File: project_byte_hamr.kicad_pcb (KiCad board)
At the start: 4 copper layers, 125.8 x 84.7 mm, 93 parts, among them J3 Bus_Apple_II_Card_Side, J4 CONN_02X03, U1 LFE5U-25F-6BG381C, U10 IS25LP128F-JBLE, U11 SN74LVC8T245, U12 SN74LVC8T245, U13 SN74LVC8T245, U14 SN74LVC8T245, U2 MT48LC16M16A2TG, U3 TLV62569DBV, U4 TLV62569DBV, U5 TLV62569DBV, U6 FT231XQ, U8 SN74LVC8T245, U9 SN74LVC8T245, Y1 FNETHE025

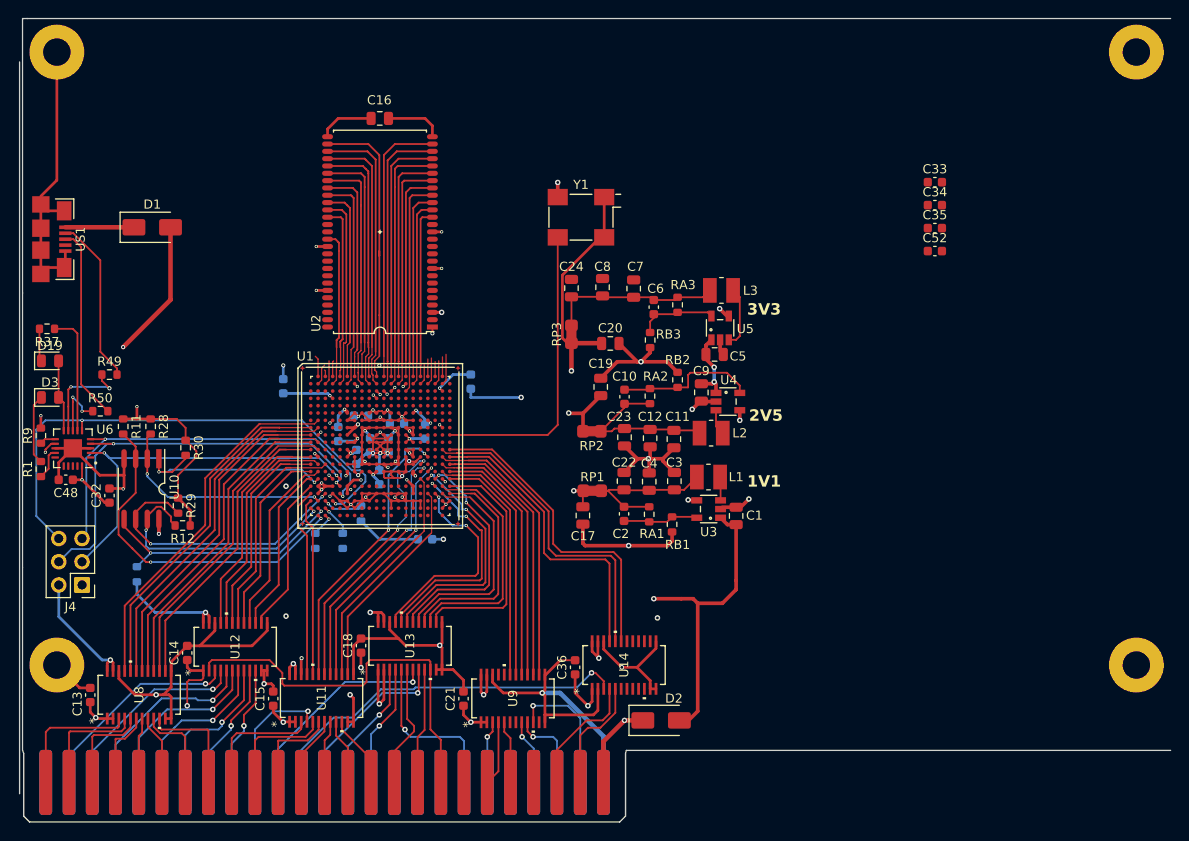
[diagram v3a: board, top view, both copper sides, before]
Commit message: Constraint Fixes
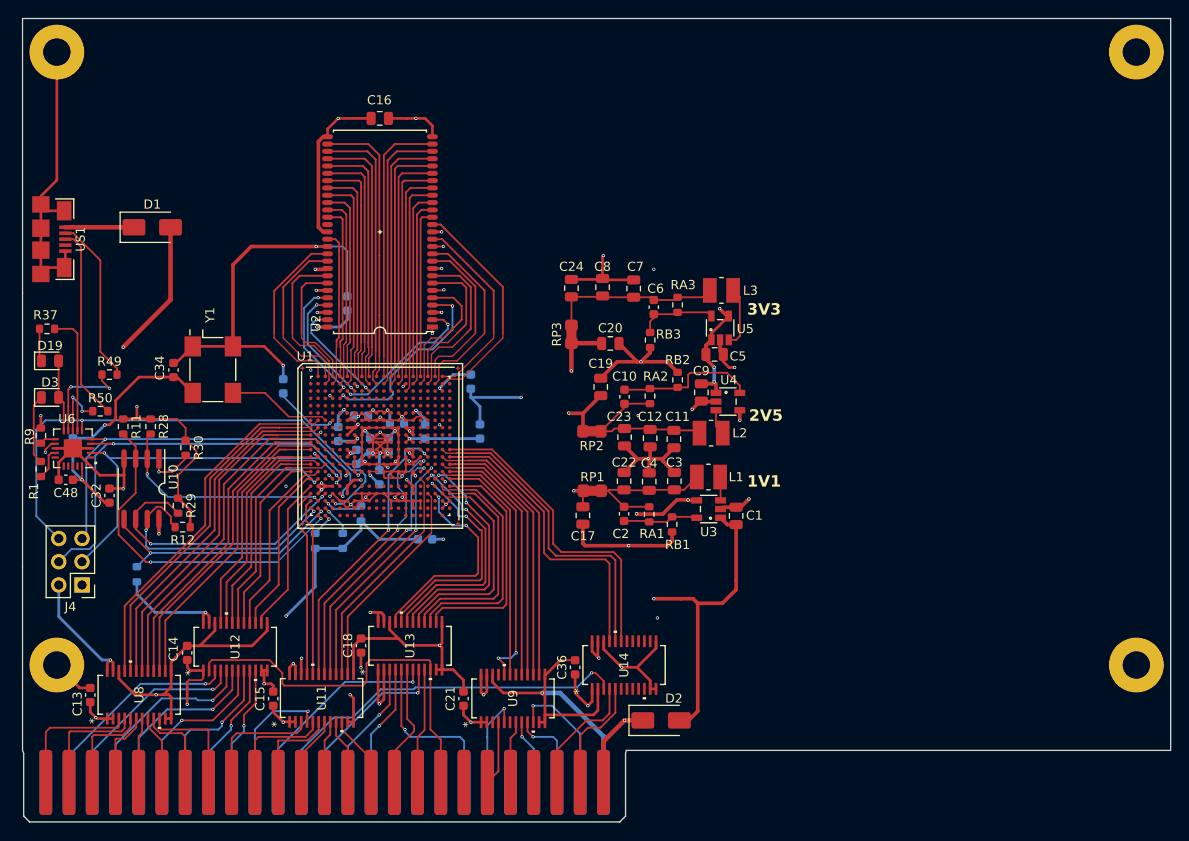
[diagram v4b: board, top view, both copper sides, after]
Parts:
- C33, C35, C52: moved to B.Cu
- moved C35 97.2 mm to (55.5, 96.7), turned to 90 degrees
- moved C34 85.2 mm to (66.5, 88.5), turned to -90 degrees
- moved C52 64.5 mm to (85.5, 81.2), turned to -90 degrees
- moved C33 56.7 mm to (100.0, 95.2), turned to -90 degrees
- moved Y1 43.6 mm to (70.8, 88.5), turned to -90 degrees
- moved R12 0.17 mm to (67.5, 105.7)
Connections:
- U1 pad A17: unconnected-(U1B-PT116A-PadA17) -> SDRAM_D3
- U1 pad A18: unconnected-(U1B-PT119A-PadA18) -> SDRAM_D5
- U1 pad A19: unconnected-(U1B-PT121A-PadA19) -> SDRAM_D7
- U1 pad A2: unconnected-(U1F-PL35A-PadA2) -> SDRAM_D9
- U1 pad A3: unconnected-(U1F-PL14C-PadA3) -> SDRAM_D10
- U1 pad A4: unconnected-(U1F-PL11A-PadA4) -> SDRAM_D12
- U1 pad B16: unconnected-(U1B-PT110B-PadB16) -> SDRAM_D2
- U1 pad B17: unconnected-(U1B-PT114A-PadB17) -> SDRAM_D4
- U1 pad B18: unconnected-(U1B-PT116B-PadB18) -> SDRAM_D6
- U1 pad B19: SDRAM_D6 -> SDRAM_DQM0
- U1 pad B3: SDRAM_DQM0 -> SDRAM_D11
- U1 pad C17: SDRAM_D5 -> unconnected-(U1B-PT114B-PadC17)
- U1 pad C20: SDRAM_D11 -> unconnected-(U1C-PR35A-PadC20)
- U1 pad C5: unconnected-(U1F-PL11D-PadC5) -> SDRAM_D13
- U1 pad C6: unconnected-(U1A-PT11A-PadC6) -> SDRAM_D0
- U1 pad C7: unconnected-(U1A-PT11B-PadC7) -> SDRAM_D14
- U1 pad C9: unconnected-(U1A-PT54A-PadC9) -> SDRAM_D15
- U1 pad D13: SDRAM_D1 -> unconnected-(U1B-PT80A-PadD13)
- U1 pad D14: SDRAM_D3 -> unconnected-(U1B-PT85A-PadD14)
- U1 pad D16: SDRAM_D7 -> unconnected-(U1B-PT112B-PadD16)
- U1 pad D19: SDRAM_D10 -> unconnected-(U1C-PR35B-PadD19)
- U1 pad D20: SDRAM_D9 -> unconnected-(U1C-VREF1_2-PadD20)
- U1 pad D5: unconnected-(U1F-PL17B-PadD5) -> SDRAM_D1
- U1 pad E14: SDRAM_D2 -> unconnected-(U1B-PT85B-PadE14)
- U1 pad E15: SDRAM_D4 -> unconnected-(U1B-PT107B-PadE15)
- U1 pad E18: SDRAM_D12 -> unconnected-(U1C-PR14C-PadE18)
- U1 pad F18: SDRAM_D13 -> unconnected-(U1C-PR14D-PadF18)
- U1 pad G3: unconnected-(U1F-PCLKT7_1-PadG3) -> CLK_25MHz
- U1 pad J16: SDRAM_D0 -> unconnected-(U1C-PR20D-PadJ16)
- U1 pad J17: SDRAM_D15 -> unconnected-(U1C-PR20C-PadJ17)
- U1 pad J18: SDRAM_D14 -> unconnected-(U1C-GR_PCLK2_0-PadJ18)
- U1 pad J20: CLK_25MHz -> unconnected-(U1C-PCLKT2_0-PadJ20)
- U9 pad 18: ~{I/O_STROBE}_3V3 -> unconnected-(U9-B4-Pad18)
- U9 pad 20: unconnected-(U9-B2-Pad20) -> ~{I/O_STROBE}_3V3
- U9 pad 4: unconnected-(U9-A2-Pad4) -> ~{I/O_STROBE}_5V
- U9 pad 6: ~{I/O_STROBE}_5V -> unconnected-(U9-A4-Pad6)
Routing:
- net GND: track 348.2 -> 409.1 mm, vias 44 -> 51
- net +3V3: track 324.6 -> 378.1 mm
- net +5V: track 79.8 -> 109.8 mm, vias 8 -> 11
- net SDRAM_D1: track 0.00 -> 22.1 mm, vias 0 -> 2
- net SDRAM_DQM0: track 2.67 -> 24.8 mm
- net SDRAM_D7: track 0.00 -> 21.5 mm
- net CLK_25MHz: track 32.8 -> 11.3 mm
- net SDRAM_D9: track 0.00 -> 20.0 mm
- net SDRAM_D10: track 0.00 -> 18.8 mm
- net SDRAM_D5: track 0.00 -> 18.4 mm
- net SDRAM_D4: track 0.00 -> 18.1 mm
- net SDRAM_D11: track 0.00 -> 17.9 mm
- net SDRAM_D6: track 3.37 -> 20.7 mm
- net SDRAM_D0: track 0.00 -> 16.5 mm, vias 0 -> 2
- net SDRAM_D3: track 0.00 -> 16.1 mm
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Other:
- board size 125.8 x 84.7 mm -> 125.5 x 80.3 mm

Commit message: Added Breakout pins + logo
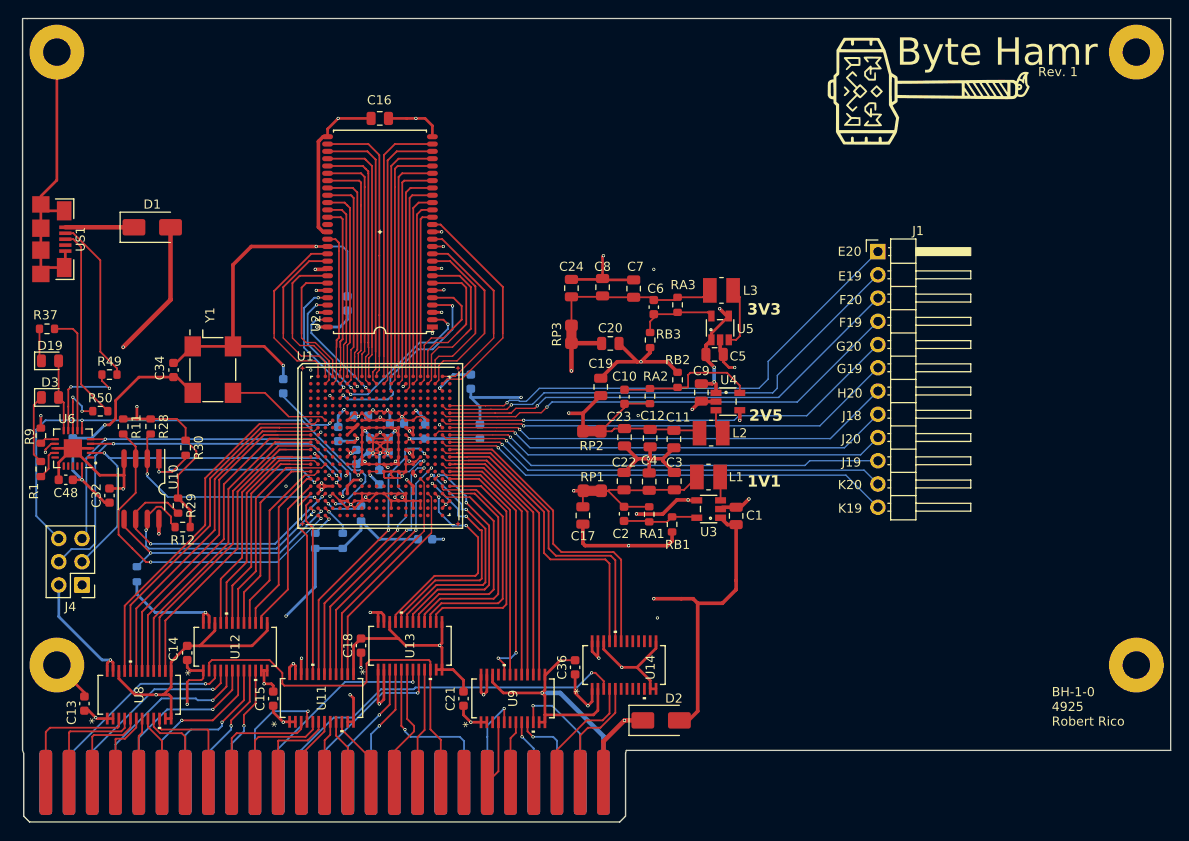
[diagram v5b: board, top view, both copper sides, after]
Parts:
- added G***: LOGO, project_byte_hamr:logo_sm, F.Cu at (149.0, 58.0)
- added J1: Conn_01x12_Socket, Connector_PinHeader_2.54mm:PinHeader_1x12_P2.54mm_Horizontal, F.Cu at (143.5, 75.6)
- moved C13 1.14 mm to (56.8, 125.0)
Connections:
- U1 pad E16: USB_FPGA_D+ -> unconnected-(U1C-PR11C-PadE16)
- U1 pad E19: unconnected-(U1C-PR35D-PadE19) -> I/O_PIN_11
- U1 pad E20: unconnected-(U1C-PR38A-PadE20) -> I/O_PIN_12
- U1 pad F16: USB_FPGA_D- -> unconnected-(U1C-PR11D-PadF16)
- U1 pad F19: unconnected-(U1C-PR38B-PadF19) -> I/O_PIN_9
- U1 pad F20: unconnected-(U1C-PR38C-PadF20) -> I/O_PIN_10
- U1 pad G19: unconnected-(U1C-GR_PCLK2_1-PadG19) -> I/O_PIN_7
- U1 pad G20: unconnected-(U1C-PR38D-PadG20) -> I/O_PIN_8
- U1 pad H20: unconnected-(U1C-PR41B-PadH20) -> I/O_PIN_6
- U1 pad J18: unconnected-(U1C-GR_PCLK2_0-PadJ18) -> I/O_PIN_5
- U1 pad J19: unconnected-(U1C-PCLKT2_1-PadJ19) -> I/O_PIN_3
- U1 pad J20: unconnected-(U1C-PCLKT2_0-PadJ20) -> I/O_PIN_4
- U1 pad K19: unconnected-(U1C-PCLKC2_1-PadK19) -> I/O_PIN_1
- U1 pad K20: unconnected-(U1C-PCLKC2_0-PadK20) -> I/O_PIN_2
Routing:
- net I/O_PIN_12: track 0.00 -> 55.0 mm, vias 0 -> 1
- net I/O_PIN_11: track 0.00 -> 54.7 mm, vias 0 -> 1
- net I/O_PIN_9: track 0.00 -> 52.1 mm, vias 0 -> 1
- net I/O_PIN_10: track 0.00 -> 52.0 mm, vias 0 -> 1
- net I/O_PIN_5: track 0.00 -> 50.8 mm, vias 0 -> 1
- net I/O_PIN_1: track 0.00 -> 50.5 mm, vias 0 -> 1
- net I/O_PIN_7: track 0.00 -> 50.5 mm, vias 0 -> 1
- net I/O_PIN_8: track 0.00 -> 50.2 mm, vias 0 -> 1
- net I/O_PIN_6: track 0.00 -> 49.5 mm, vias 0 -> 1
- net I/O_PIN_3: track 0.00 -> 49.2 mm, vias 0 -> 1
- net I/O_PIN_2: track 0.00 -> 48.7 mm, vias 0 -> 1
- net I/O_PIN_4: track 0.00 -> 48.5 mm, vias 0 -> 1
- net +3V3: vias 33 -> 32
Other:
- board text added: "BH-1-0 4925 Robert Rico"
- board text added: "Byte Hamr"
- board text added: "E19"
- board text added: "E20"
- board text added: "F19"
- board text added: "F20"
- board text added: "G19"
- board text added: "G20"
- board text added: "H20"
- board text added: "J18"
- board text added: "J19"
- board text added: "J20"
- board text added: "K19"
- board text added: "K20"
- board text added: "Rev. 1"

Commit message: Rev. 1 - Sent to Fab
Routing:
- net +3V3: track 378.1 -> 377.9 mm, vias 32 -> 33
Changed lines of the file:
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@@
-	)
-	(segment
-		(start 86.30513 94.8)
-		(end 86.662039 94.443091)
-		(width 0.4)
-		(layer "F.Cu")
-		(net 9)
 	)
 	(segment
@@
 	)
 	(segment
+		(start 85.5 95.6)
+		(end 85.5 94.8)
+		(width 0.3)
+		(layer "F.Cu")
+		(net 9)
+	)
+	(segment
 		(start 67 100)
 		(end 69 98)
@@
 		(end 112.8925 119.8925)
 		(width 0.3)
+		(layer "F.Cu")
+		(net 9)
+	)
+	(segment
+		(start 85.86936 95.23577)
+		(end 85.86936 95.23064)
+		(width 0.1525)
 		(layer "F.Cu")
 		(net 9)
@@
 	)
 	(segment
-		(start 85.606389 95.493611)
-		(end 85.5 95.493611)
-		(width 0.2)
-		(layer "F.Cu")
-		(net 9)
-	)
-	(segment
 		(start 90.222188 93.2)
 		(end 89.89543 92.873242)
@@
 	)
 	(segment
+		(start 85.86936 95.23064)
+		(end 86.3 94.8)
+		(width 0.3)
+		(layer "F.Cu")
+		(net 9)
+	)
+	(segment
 		(start 87.9 93.2)
 		(end 87.972772 93.2)
@@
 		(end 95.818721 73.394365)
 		(width 0.2)
-		(layer "F.Cu")
-		(net 9)
-	)
-	(segment
-		(start 86.3 94.8)
-		(end 85.606389 95.493611)
-		(width 0.3)
 		(layer "F.Cu")
 		(net 9)
@@
 		(net 9)
 	)
+	(via
+		(at 85.86936 95.23577)
+		(size 0.35)
+		(drill 0.2)
+		(layers "F.Cu" "B.Cu")
+		(net 9)
+	)

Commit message: Revision 1.0
Revision 1.0 - Sent to Fab
Latest BOM and Gerbers+Drill in .zip
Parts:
- removed J1: Conn_01x12_Socket, Connector_PinHeader_2.54mm:PinHeader_1x12_P2.54mm_Horizontal
- added J2: Conn_01x13_Socket, Connector_PinHeader_2.54mm:PinHeader_1x13_P2.54mm_Horizontal, F.Cu at (143.5, 75.5)
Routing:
- net GND: track 409.1 -> 412.0 mm, vias 51 -> 52
